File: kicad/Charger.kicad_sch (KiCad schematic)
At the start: 34 parts, among them U10 BQ25672RQMR

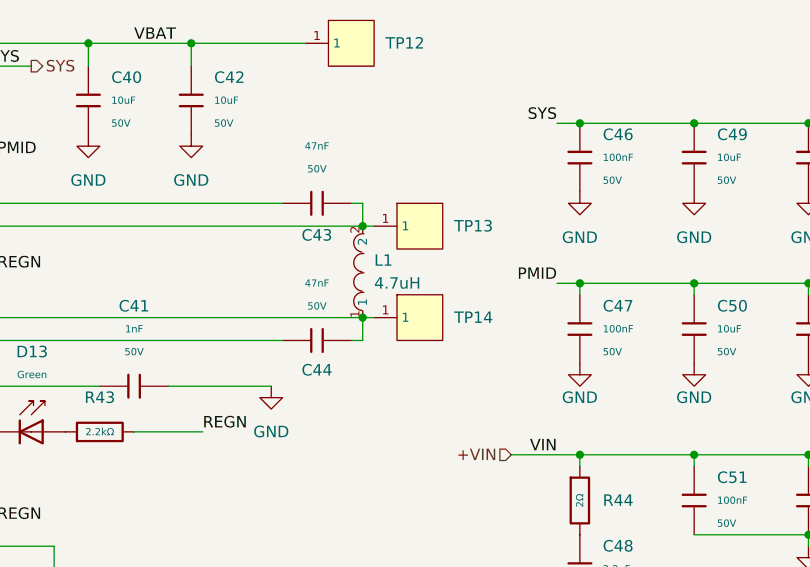
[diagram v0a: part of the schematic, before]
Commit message: Charger IC footprint routed RP2040 routed BMS routed xt30s and balancers router
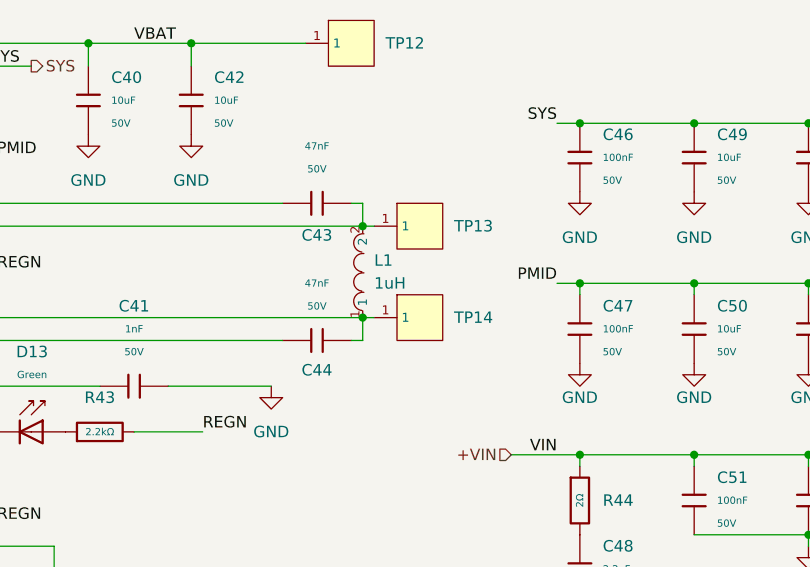
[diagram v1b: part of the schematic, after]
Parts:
- L1: value 4.7uH -> 1uH
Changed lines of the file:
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@@
 			)
 		)
-		(property "Value" "4.7uH"
+		(property "Value" "1uH"
 			(at 139.7 58.4199 90)
 			(effects
